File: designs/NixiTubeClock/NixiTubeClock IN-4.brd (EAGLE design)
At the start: 59 x 98 mm, 15 parts, among them IC1 74141N, IC2 74HCT595D, IC3 74141N, IC4 74141N, IC5 74HCT595D, IC6 74141N

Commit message: added first IN-4 Design and edited mainboard to fit all screws for IN-4
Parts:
- removed AN1, AN2, AN3, AN4: ZM1000, NixieTube:ZM1000
- added N1, N2, N3, N4: IN-4, NixieTube:IN-18
- moved R4 277.7 mm to (3.00, -250.0), flipped to the top, turned to 0 degrees
- moved R1 252.2 mm to (3.00, -172.0), flipped to the top
- moved R3 243.4 mm to (3.00, -211.0), flipped to the top, turned to 0 degrees
- moved R2 210.3 mm to (3.00, -133.0), flipped to the top
- moved IC3 45.4 mm to (13.0, 127.0)
- moved IC1 26.7 mm to (13.0, 94.0)
- moved IC2 23.4 mm to (19.0, 76.5)
- moved IC5 21.5 mm to (19.0, 63.5)
- moved SV1 21.0 mm to (3.00, 70.0)
- moved IC4 17.1 mm to (13.0, 46.0)
- moved IC6 6.71 mm to (13.0, 13.0)
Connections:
- removed net N$100: AN4.A, R4.1
- removed net N$13: AN1.2, IC1.8
- removed net N$15: AN1.3, IC1.9
- removed net N$16: AN1.4, IC1.13
- removed net N$17: AN1.5, IC1.14
- removed net N$18: AN1.6, IC1.11
- removed net N$19: AN1.7, IC1.10
- removed net N$20: AN1.8, IC1.1
- removed net N$21: AN1.9, IC1.2
- removed net N$22: AN2.0, IC3.16
- removed net N$23: AN2.1, IC3.15
- removed net N$24: AN2.2, IC3.8
- removed net N$25: AN2.3, IC3.9
- removed net N$26: AN2.4, IC3.13
- removed net N$27: AN2.5, IC3.14
- removed net N$28: AN2.6, IC3.11
- removed net N$29: AN2.7, IC3.10
- removed net N$30: AN2.8, IC3.1
- removed net N$31: AN2.9, IC3.2
- removed net N$32: AN3.0, IC4.16
- removed net N$35: AN3.1, IC4.15
- removed net N$36: AN3.2, IC4.8
- removed net N$66: AN3.3, IC4.9
- removed net N$67: AN3.4, IC4.13
- removed net N$68: AN3.5, IC4.14
- removed net N$69: AN3.6, IC4.11
- removed net N$70: AN3.7, IC4.10
- removed net N$71: AN3.8, IC4.1
- removed net N$72: AN3.9, IC4.2
- removed net N$73: AN4.0, IC6.16
- removed net N$74: AN4.1, IC6.15
- removed net N$75: AN4.2, IC6.8
- removed net N$76: AN4.3, IC6.9
- removed net N$9: AN1.1, IC1.15
- removed net N$91: AN4.4, IC6.13
- removed net N$92: AN4.5, IC6.14
- removed net N$93: AN4.6, IC6.11
- removed net N$94: AN4.7, IC6.10
- removed net N$95: AN4.8, IC6.1
- removed net N$96: AN4.9, IC6.2
- removed net N$97: AN1.A, R2.1
- removed net N$98: AN2.A, R1.1
- removed net N$99: AN3.A, R3.1
- new net DRIVER_0_0: IC1.16, N1.N/C2
- new net DRIVER_0_1: IC3.16, N2.N/C2
- new net DRIVER_0_2: IC4.16, N3.N/C2
- new net DRIVER_0_3: IC6.16, N4.N/C2
- new net DRIVER_1_0: IC1.15, N1.9
- new net DRIVER_1_1: IC3.15, N2.9
- new net DRIVER_1_2: IC4.15, N3.9
- new net DRIVER_1_3: IC6.15, N4.9
- new net DRIVER_2_0: IC1.8, N1.8
- new net DRIVER_2_1: IC3.8, N2.8
- new net DRIVER_2_2: IC4.8, N3.8
- new net DRIVER_2_3: IC6.8, N4.8
- new net DRIVER_3_0: IC1.9, N1.1
- new net DRIVER_3_1: IC3.9, N2.1
- new net DRIVER_3_2: IC4.9, N3.1
- new net DRIVER_3_3: IC6.9, N4.1
- new net DRIVER_4_0: IC1.13, N1.N/C
- new net DRIVER_4_1: IC3.13, N2.N/C
- new net DRIVER_4_2: IC4.13, N3.N/C
- new net DRIVER_4_3: IC6.13, N4.N/C
- new net DRIVER_5_0: IC1.14, N1.A2
- new net DRIVER_5_1: IC3.14, N2.A2
- new net DRIVER_5_2: IC4.14, N3.A2
- new net DRIVER_5_3: IC6.14, N4.A2
- new net DRIVER_6_0: IC1.11, N1.4
- new net DRIVER_6_1: IC3.11, N2.4
- new net DRIVER_6_2: IC4.11, N3.4
- new net DRIVER_6_3: IC6.11, N4.4
- new net DRIVER_7_0: IC1.10, N1.7
- new net DRIVER_7_1: IC3.10, N2.7
- new net DRIVER_7_2: IC4.10, N3.7
- new net DRIVER_7_3: IC6.10, N4.7
- new net DRIVER_8_0: IC1.1, N1.5
- new net DRIVER_8_1: IC3.1, N2.5
- new net DRIVER_8_2: IC4.1, N3.5
- new net DRIVER_8_3: IC6.1, N4.5
- new net DRIVER_9_0: IC1.2, N1.6
- new net DRIVER_9_1: IC3.2, N2.6
- new net DRIVER_9_2: IC4.2, N3.6
- new net DRIVER_9_3: IC6.2, N4.6
- new net N$12: N1.0, R2.1
- new net N$4: N2.0, R1.1
- new net N$5: N3.0, R3.1
- net N$7: now also N4.0, R4.1; no longer AN1.0, IC1.16
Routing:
- net GND: track 147.6 -> 257.4 mm, vias 7 -> 0
- net N$114: track 71.0 -> 0.00 mm
- net N$115: track 48.2 -> 118.5 mm, vias 1 -> 0
- net 170V: track 122.0 -> 181.1 mm, vias 4 -> 0
- net N$116: track 29.3 -> 81.2 mm, vias 3 -> 0
- net N$66: track 45.3 -> 0.00 mm
- net N$13: track 45.1 -> 0.00 mm
- net N$70: track 45.0 -> 0.00 mm
- net SH_CP: track 44.6 -> 0.00 mm
- net N$105: track 33.9 -> 78.0 mm, vias 1 -> 0
- net N$75: track 43.8 -> 0.00 mm
- net N$36: track 42.3 -> 0.00 mm
- net N$113: track 46.4 -> 88.7 mm, vias 2 -> 0
- net N$24: track 42.0 -> 0.00 mm
- net N$25: track 40.7 -> 0.00 mm
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- removed copper zone on layer 1, net GND
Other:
- board size 59 x 98 mm -> 59 x 140 mm

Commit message: improved design of IN-4
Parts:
- moved R1 276.6 mm to (21.0, 104.0), flipped to the bottom
- moved R4 273.6 mm to (21.0, 23.0), flipped to the bottom
- moved R2 270.6 mm to (21.0, 137.0), flipped to the bottom
- moved R3 267.6 mm to (21.0, 56.0), flipped to the bottom
- turned N1 to 25 degrees
- turned N2 to 25 degrees
- turned N3 to 25 degrees
- turned N4 to 25 degrees
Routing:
- net GND: track 257.4 -> 0.00 mm
- net 170V: track 181.1 -> 0.00 mm
- net 5V: track 145.5 -> 0.00 mm
- net N$115: track 118.5 -> 0.00 mm
- net N$113: track 88.7 -> 0.00 mm
- net N$116: track 81.2 -> 0.00 mm
- net N$105: track 78.0 -> 0.00 mm
- net N$106: track 55.9 -> 0.00 mm
- net DS: track 47.5 -> 0.00 mm
- net N$1: track 47.3 -> 0.00 mm
- net N$107: track 45.5 -> 0.00 mm
- net N$108: track 45.2 -> 0.00 mm
- net N$110: track 39.8 -> 0.00 mm
- net N$101: track 39.2 -> 0.00 mm
- net N$109: track 36.0 -> 0.00 mm
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- added copper zone on layer 1, net GND

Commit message: added new design in brd from NI-4
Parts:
- flipped IC2 to the bottom, turned to 0 degrees
- flipped IC5 to the bottom, turned to 0 degrees
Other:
- board text added: "Bösenberg"
- board text added: "Moritz"
- board text removed: "Moritz Bösenberg"

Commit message: added new design in brd from NI-4
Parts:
- moved IC6 114.0 mm to (13.0, 127.0)
- moved IC1 81.0 mm to (13.0, 13.0)
- moved IC3 81.0 mm to (13.0, 46.0)
- moved IC4 48.0 mm to (13.0, 94.0)

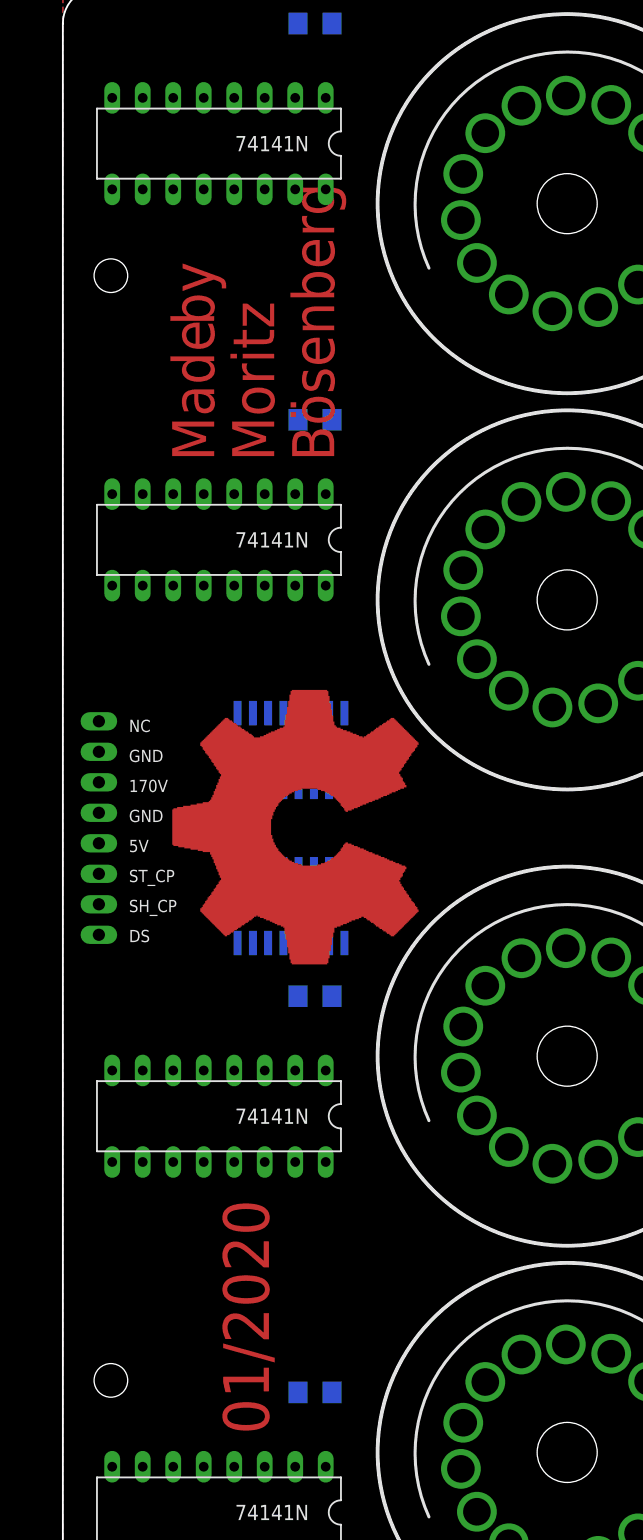
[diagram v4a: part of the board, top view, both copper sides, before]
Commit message: worked on routing in IN4
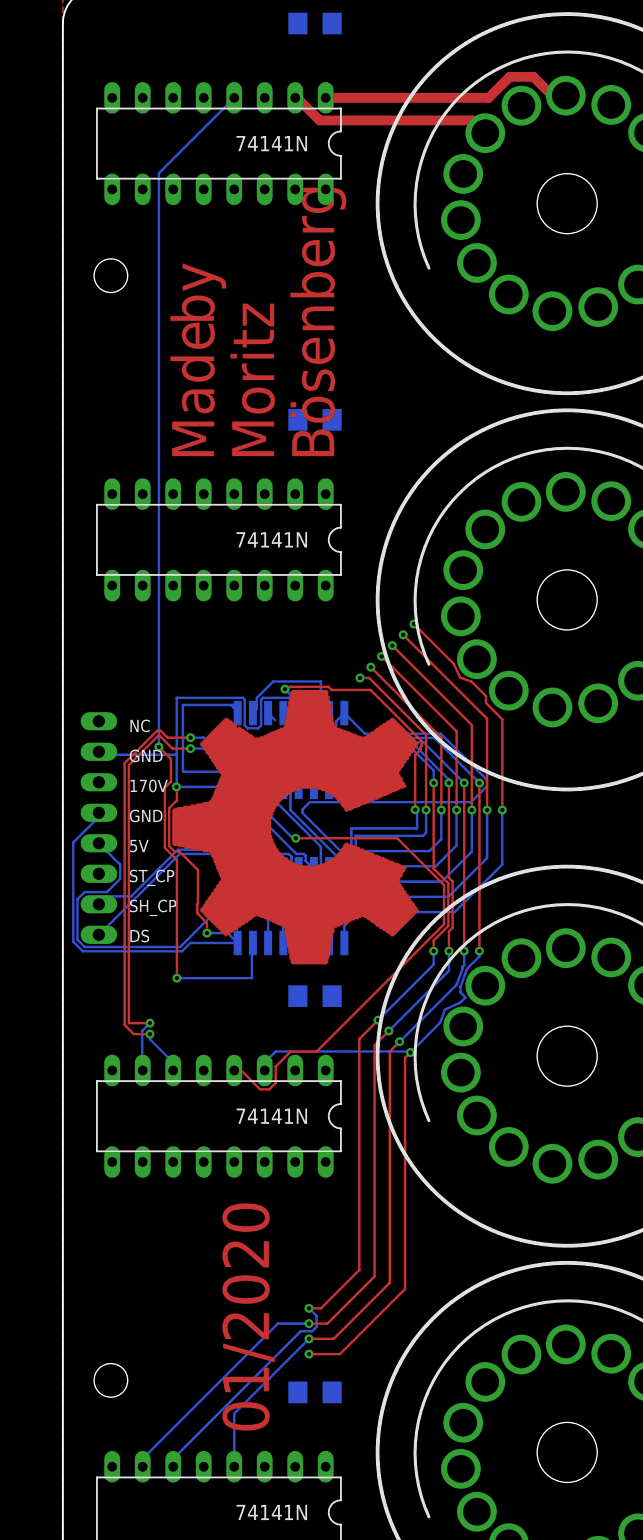
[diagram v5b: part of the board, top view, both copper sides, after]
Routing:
- net N$105: track 0.00 -> 88.3 mm, vias 0 -> 4
- net N$116: track 0.00 -> 86.2 mm, vias 0 -> 2
- net N$103: track 0.00 -> 84.3 mm, vias 0 -> 4
- net N$104: track 0.00 -> 82.7 mm, vias 0 -> 4
- net N$102: track 0.00 -> 80.9 mm, vias 0 -> 4
- net 5V: track 0.00 -> 80.2 mm
- net GND: track 0.00 -> 77.7 mm, vias 0 -> 2
- net DS: track 0.00 -> 62.2 mm, vias 0 -> 2
- net N$108: track 0.00 -> 47.8 mm, vias 0 -> 1
- net N$106: track 0.00 -> 45.9 mm, vias 0 -> 2
- net N$107: track 0.00 -> 43.0 mm, vias 0 -> 2
- net N$110: track 0.00 -> 39.9 mm, vias 0 -> 2
- net N$111: track 0.00 -> 38.7 mm, vias 0 -> 2
- net N$1: track 0.00 -> 38.1 mm, vias 0 -> 2
- net N$114: track 0.00 -> 37.2 mm, vias 0 -> 2
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
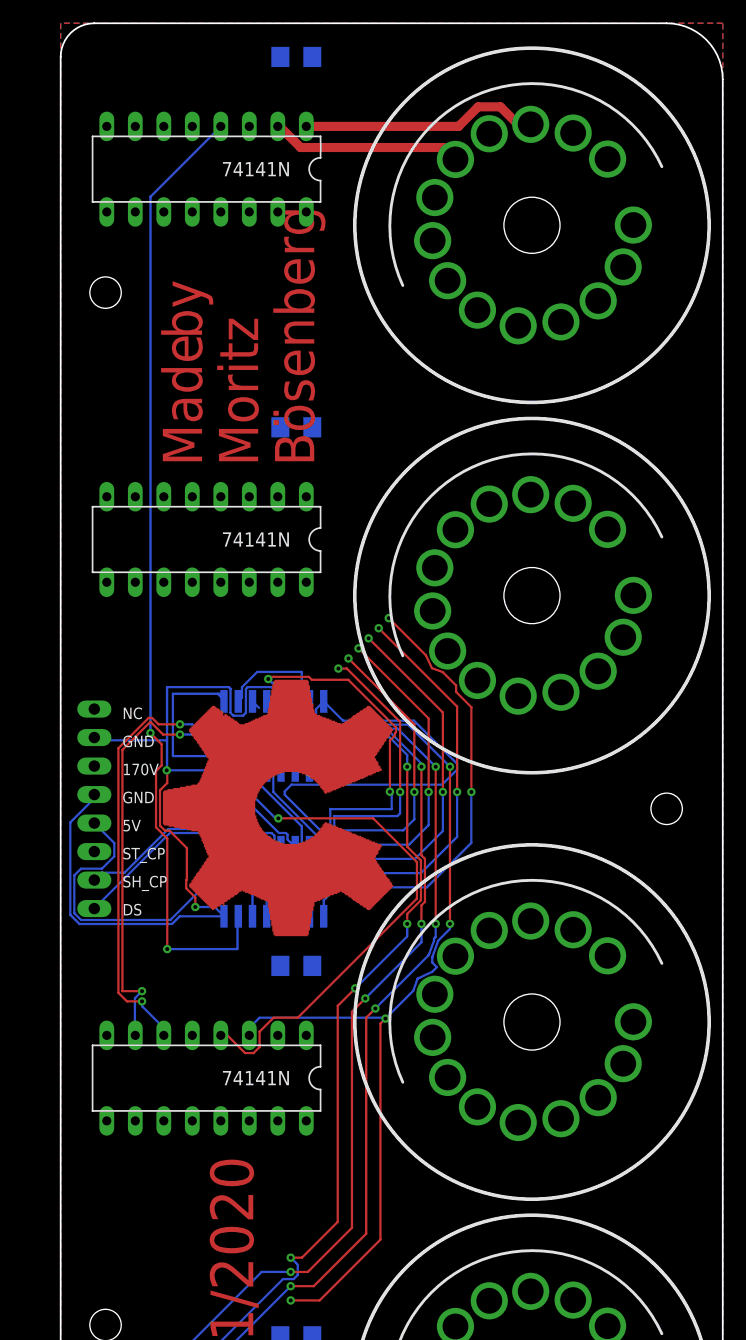
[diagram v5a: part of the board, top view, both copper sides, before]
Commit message: worked on routing in IN4
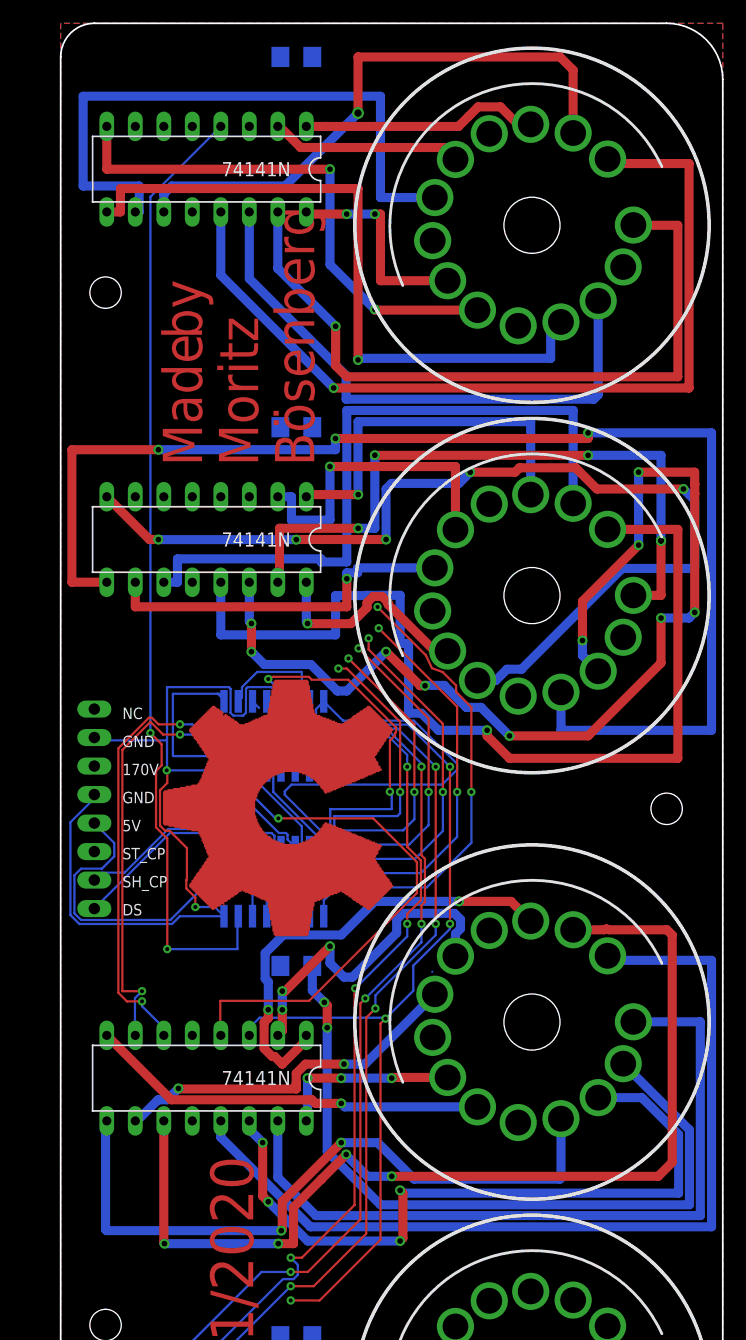
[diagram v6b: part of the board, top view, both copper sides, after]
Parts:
- moved R2 114.0 mm to (21.0, 23.0)
- moved R4 114.0 mm to (21.0, 137.0)
- moved R1 48.0 mm to (21.0, 56.0)
- moved R3 48.0 mm to (21.0, 104.0)
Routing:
- net DRIVER_3_2: track 0.00 -> 116.8 mm, vias 0 -> 3
- net DRIVER_5_2: track 0.00 -> 96.6 mm, vias 0 -> 10
- net DRIVER_6_1: track 0.00 -> 92.1 mm, vias 0 -> 4
- net DRIVER_2_2: track 0.00 -> 90.1 mm, vias 0 -> 5
- net DRIVER_4_2: track 0.00 -> 88.1 mm, vias 0 -> 1
- net DRIVER_4_1: track 0.00 -> 81.7 mm
- net DRIVER_4_3: track 0.00 -> 79.0 mm, vias 0 -> 1
- net DRIVER_1_1: track 0.00 -> 67.3 mm
- net N$4: track 0.00 -> 66.4 mm, vias 0 -> 2
- net DRIVER_5_1: track 0.00 -> 64.5 mm, vias 0 -> 4
- net DRIVER_1_3: track 0.00 -> 64.2 mm, vias 0 -> 1
- net DRIVER_3_1: track 0.00 -> 61.8 mm, vias 0 -> 2
- net DRIVER_3_3: track 0.00 -> 61.2 mm, vias 0 -> 1
- net DRIVER_6_2: track 0.00 -> 60.6 mm
- net DRIVER_1_2: track 0.00 -> 60.5 mm, vias 0 -> 5
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
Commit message: worked on brd layout NI-4
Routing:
- net 170V: track 0.00 -> 216.1 mm, vias 1 -> 14
- net N$101: track 0.00 -> 158.9 mm, vias 0 -> 6
- net 5V: track 80.2 -> 175.6 mm, vias 0 -> 6
- net N$113: track 36.9 -> 124.8 mm, vias 2 -> 6
- net GND: track 77.7 -> 163.7 mm, vias 2 -> 4
- net DRIVER_4_0: track 0.00 -> 81.9 mm
- net N$115: track 37.2 -> 116.1 mm, vias 2 -> 3
- net N$114: track 37.2 -> 113.3 mm, vias 2 -> 4
- net N$12: track 0.00 -> 69.4 mm
- net DRIVER_6_0: track 0.00 -> 68.2 mm, vias 0 -> 1
- net DRIVER_1_0: track 0.00 -> 65.2 mm
- net N$5: track 0.00 -> 61.8 mm, vias 0 -> 2
- net DRIVER_3_0: track 0.00 -> 54.3 mm, vias 0 -> 2
- net N$7: track 0.00 -> 53.7 mm
- net DRIVER_5_0: track 0.00 -> 48.8 mm, vias 0 -> 2
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
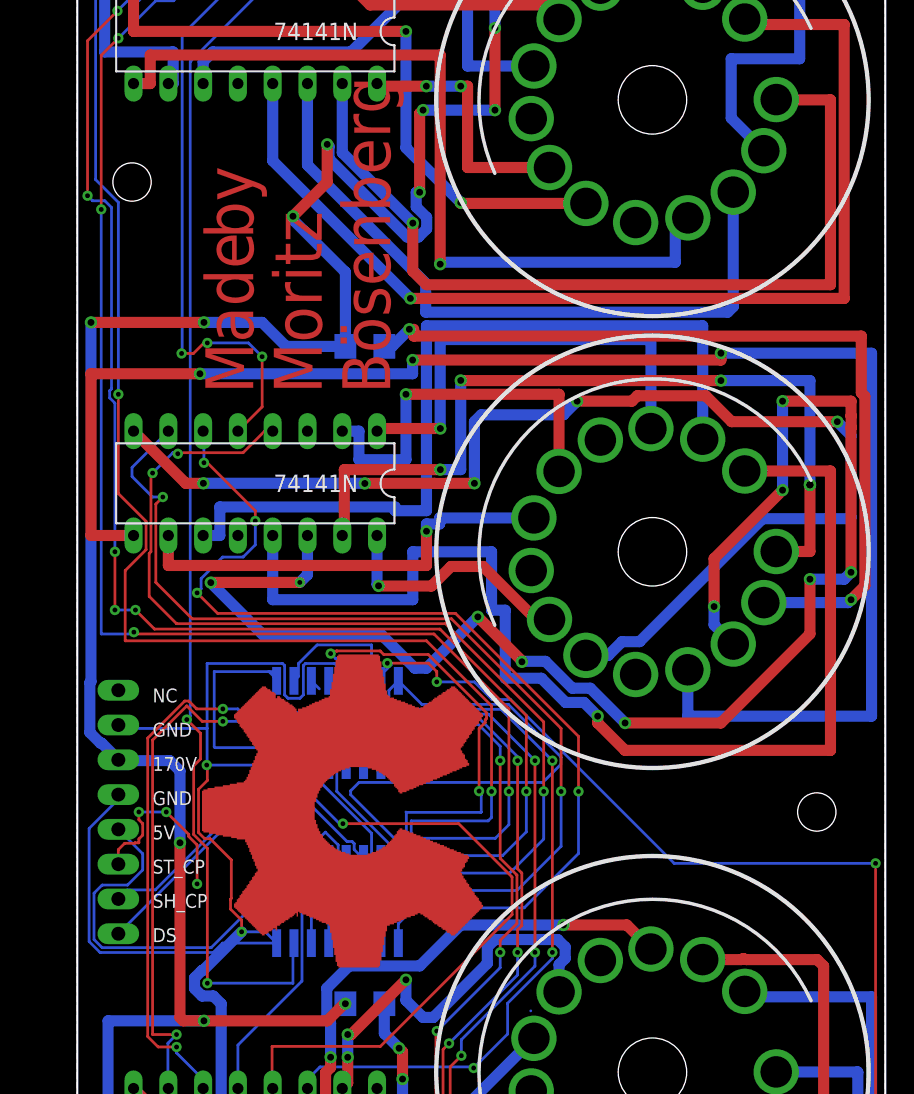
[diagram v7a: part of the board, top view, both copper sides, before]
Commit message: final review of design and ordered from JLC PCB
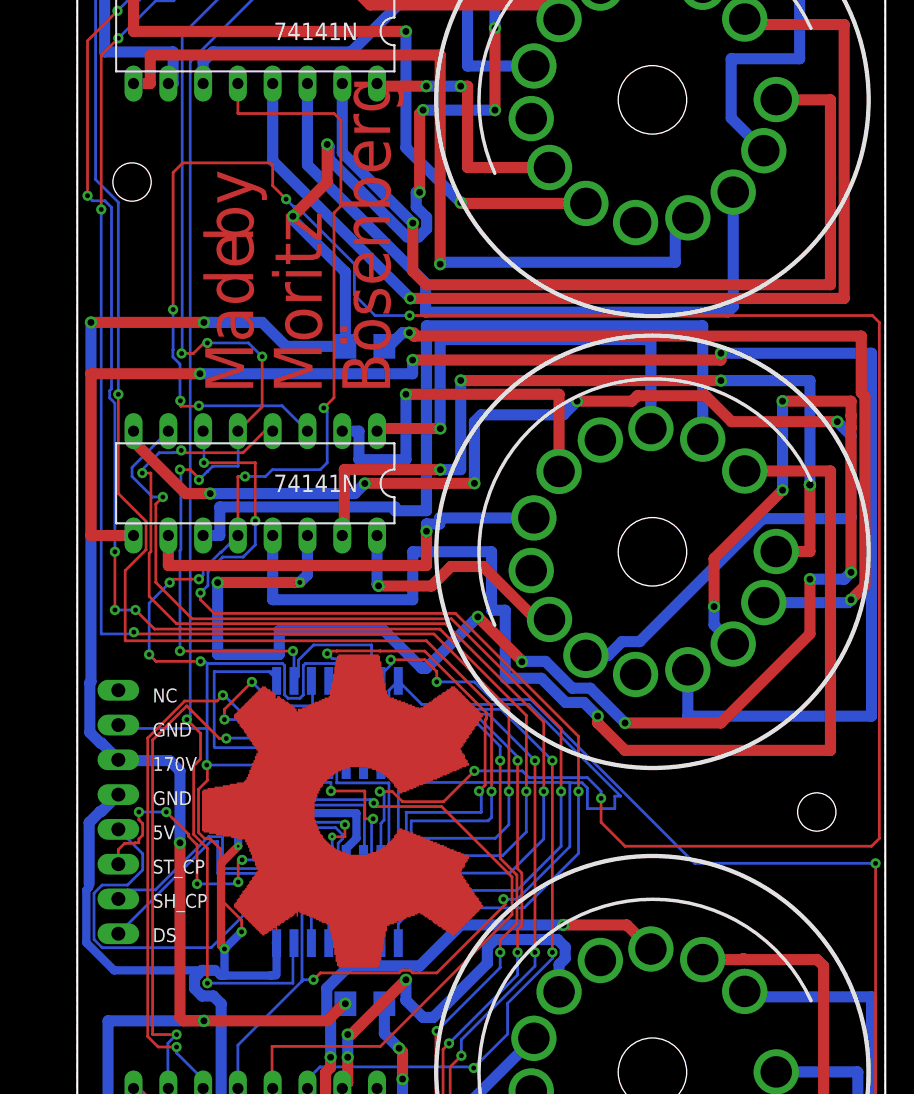
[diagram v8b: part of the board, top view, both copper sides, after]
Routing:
- net N$109: track 0.25 -> 171.3 mm, vias 0 -> 8
- net GND: track 163.7 -> 250.8 mm, vias 4 -> 12
- net 5V: track 175.6 -> 242.9 mm, vias 6 -> 12
- net SH_CP: track 37.0 -> 65.3 mm, vias 0 -> 4
- net ST_CP: track 35.2 -> 56.5 mm, vias 3 -> 7
- net DRIVER_5_2: track 109.1 -> 113.7 mm
- net DS: track 65.1 -> 68.0 mm
- net SHIFT_DATA: track 26.7 -> 28.8 mm
- net N$110: track 73.6 -> 75.6 mm
- net N$1: track 78.5 -> 80.1 mm
- net DRIVER_2_2: track 90.0 -> 91.1 mm
